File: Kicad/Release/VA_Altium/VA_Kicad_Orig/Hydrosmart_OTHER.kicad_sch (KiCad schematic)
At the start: 6 parts, among them IC1 24FC04HT-I/OT, J2 DNP, U3 CT8122AM-IS3, U4 CT8122AM-IS3

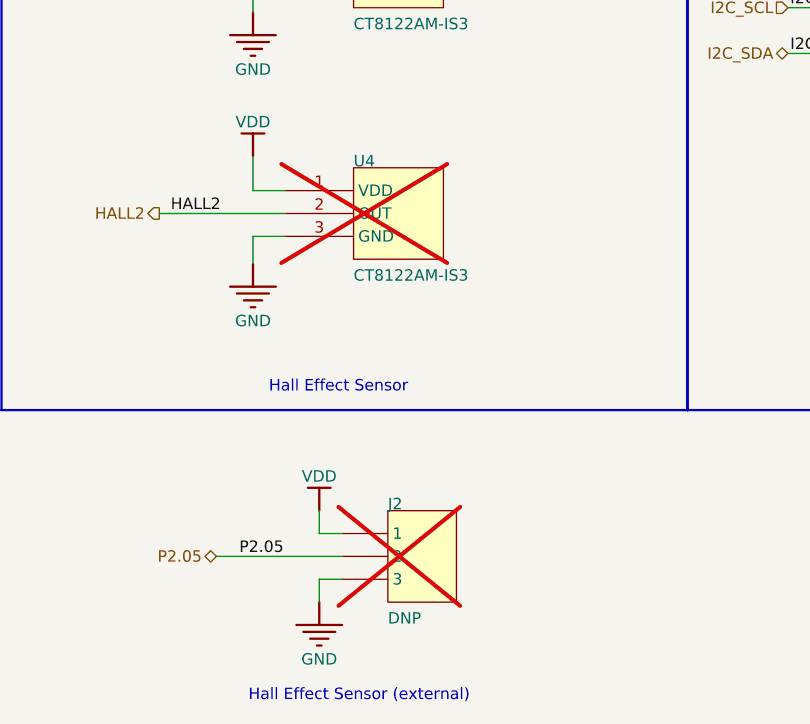
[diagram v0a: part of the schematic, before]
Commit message: VB changes start. Updated regulator and added test points
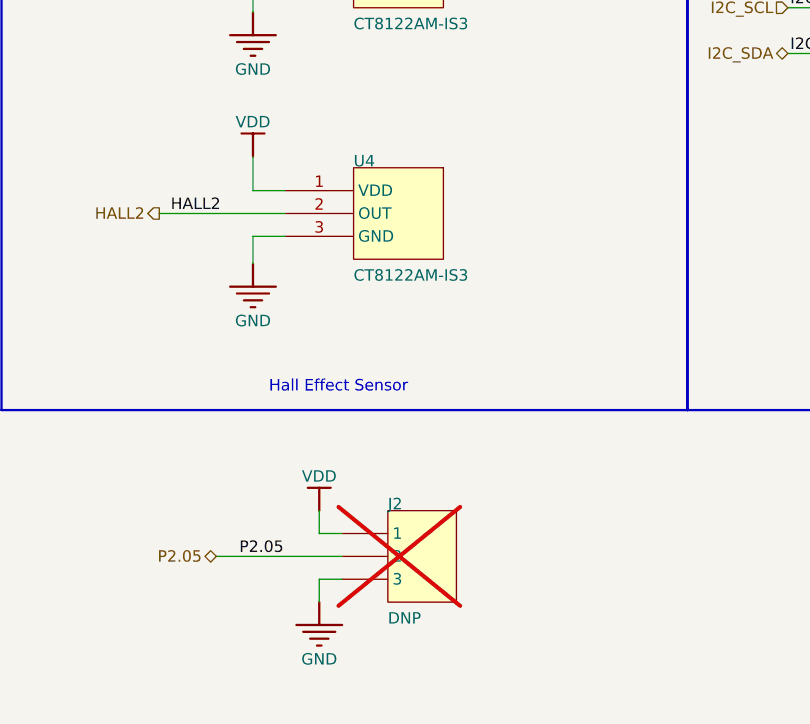
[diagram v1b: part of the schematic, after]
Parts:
- U4: now fitted; now in the parts list
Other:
- note removed: "Hall Effect Sensor (external)"
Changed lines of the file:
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@@
-		)
-	)
-	(text "Hall Effect Sensor (external)"
-		(exclude_from_sim no)
-		(at 89.916 158.496 0)
-		(effects
-			(font
-				(size 1.27 1.27)
-			)
-			(justify left bottom)
 		)
 	)
@@
 		(unit 1)
 		(exclude_from_sim no)
-		(in_bom no)
+		(in_bom yes)
 		(on_board yes)
-		(dnp yes)
+		(dnp no)
 		(property "Reference" "U4"
 			(at 101.6 99.06 0)
